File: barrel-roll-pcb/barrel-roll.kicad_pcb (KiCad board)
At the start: 2 copper layers, 51.9 x 25.2 mm, 12 parts, among them M1 Motor_DC, M2 Motor_DC, U1 XIAO-RP2040-DIP, U2 DRV8833PW, U3 WeaponMotor, U4 Recever

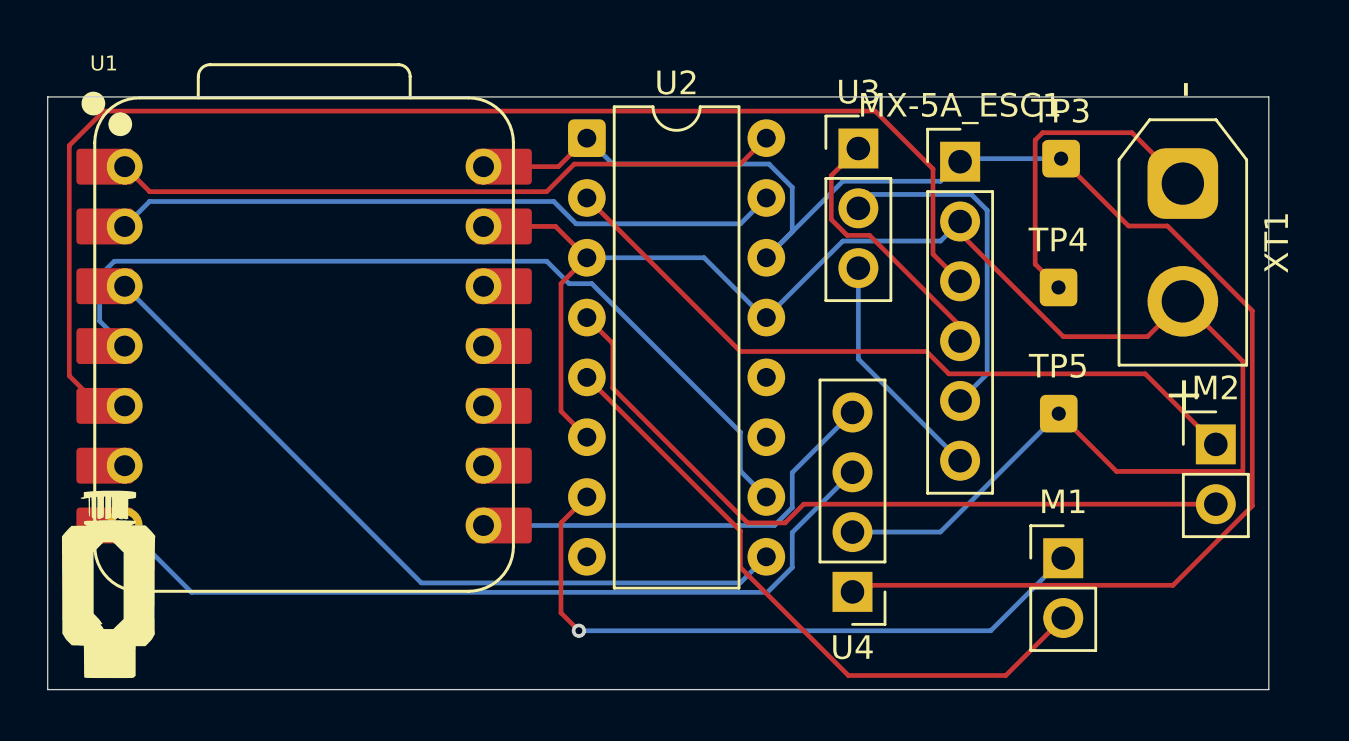
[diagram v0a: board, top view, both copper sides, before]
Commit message: Updated PCB to have a DIP version and improved readme.
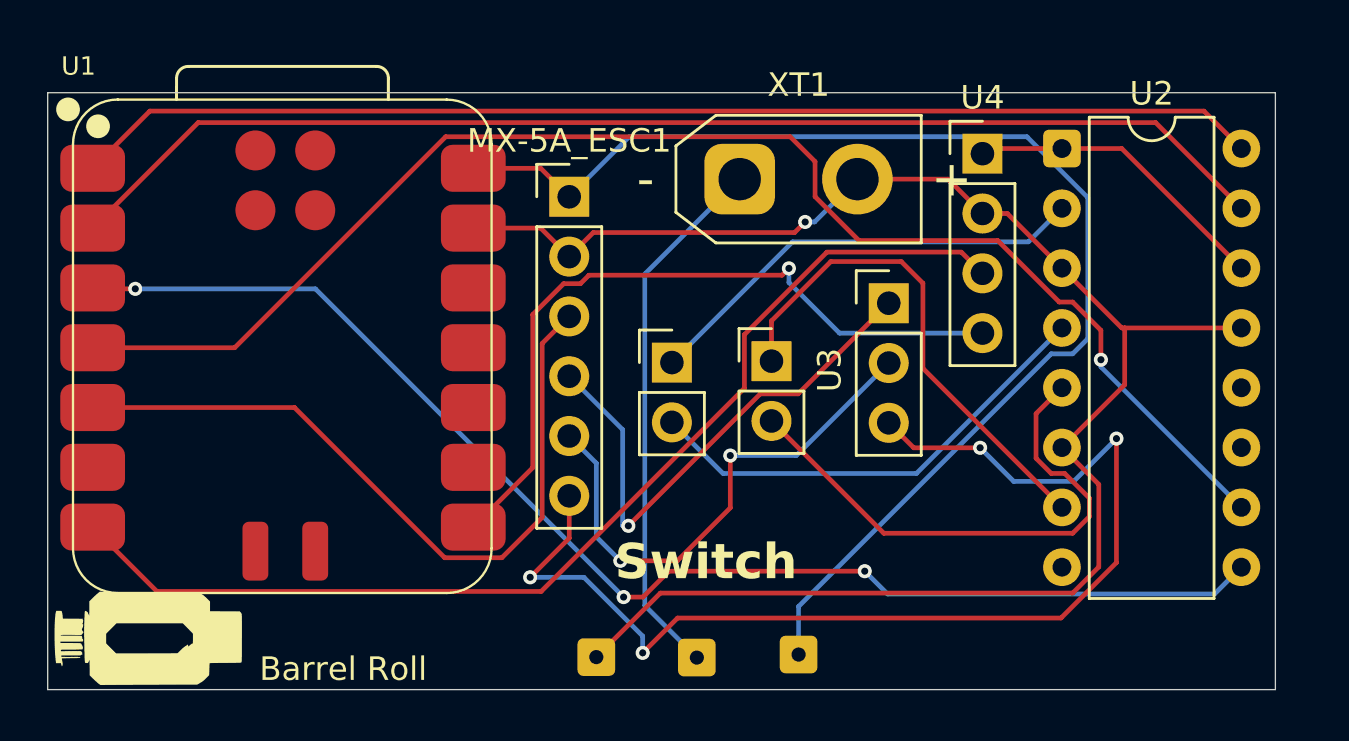
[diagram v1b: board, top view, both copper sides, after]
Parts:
- U1: footprint Seeed Studio XIAO Series Library:XIAO-RP2040-DIP -> Seeed Studio XIAO Series Library:XIAO-RP2040-SMD
- moved TP3 23.8 mm to (131.9, 53.5)
- moved M2 23.4 mm to (126.5, 41.1)
- moved TP5 22.2 mm to (123.3, 53.7)
- moved TP4 22.0 mm to (127.6, 53.7)
- moved U2 20.2 mm to (143.1, 32.1)
- moved U4 19.4 mm to (139.7, 32.3), turned to 0 degrees
- moved XT1 18.8 mm to (129.4, 33.4), turned to 0 degrees
- moved MX-5A_ESC1 16.7 mm to (122.2, 34.1)
- moved M1 15.0 mm to (130.8, 41.1)
- moved U3 6.70 mm to (135.8, 38.6)
- moved G*** 6.08 mm to (103.5, 55.0), turned to 90 degrees
- moved U1 0.98 mm to (109.9, 40.5)
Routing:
- net Net-(MX-5A_ESC1-M3): track 9.97 -> 49.1 mm, vias 0 -> 4
- net Net-(MX-5A_ESC1-SIG): track 56.2 -> 31.5 mm
- net BIN2: track 37.1 -> 60.8 mm, vias 0 -> 1
- net AIN2: track 28.5 -> 52.1 mm
- net BIN1: track 32.9 -> 55.6 mm, vias 0 -> 3
- net AIN1: track 28.6 -> 50.5 mm
- net Net-(U1-GPIO1/RX): track 18.5 -> 31.5 mm, vias 0 -> 1
- net AOUT1: track 31.0 -> 19.3 mm
- net AOUT2: track 31.8 -> 20.0 mm
- net Net-(U1-GPIO0/TX): track 35.1 -> 46.6 mm
- net Net-(MX-5A_ESC1-M1): track 11.5 -> 22.5 mm, vias 0 -> 1
- net Net-(XT1-Power): track 14.0 -> 22.9 mm
- net Net-(MX-5A_ESC1-M2): track 14.6 -> 22.4 mm, vias 0 -> 2
- net BOUT1: track 28.3 -> 21.5 mm, vias 1 -> 0
- net BT1P: track 71.5 -> 66.9 mm
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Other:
- board size 51.9 x 25.2 mm -> 52.1 x 25.3 mm
- board text added: "Switch"
- board text removed: "150g combat robot"
